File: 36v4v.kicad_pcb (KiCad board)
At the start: 2 copper layers, 85.1 x 48 mm, 47 parts, among them J1 Conn_01x03, J2 Conn_01x02, J3 Conn_01x02, J4 Conn_01x02, J5 Conn_01x02, J6 Conn_01x02, J7 Conn_01x02, U1 InnoSwitch3-CE, INN3162C, inS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

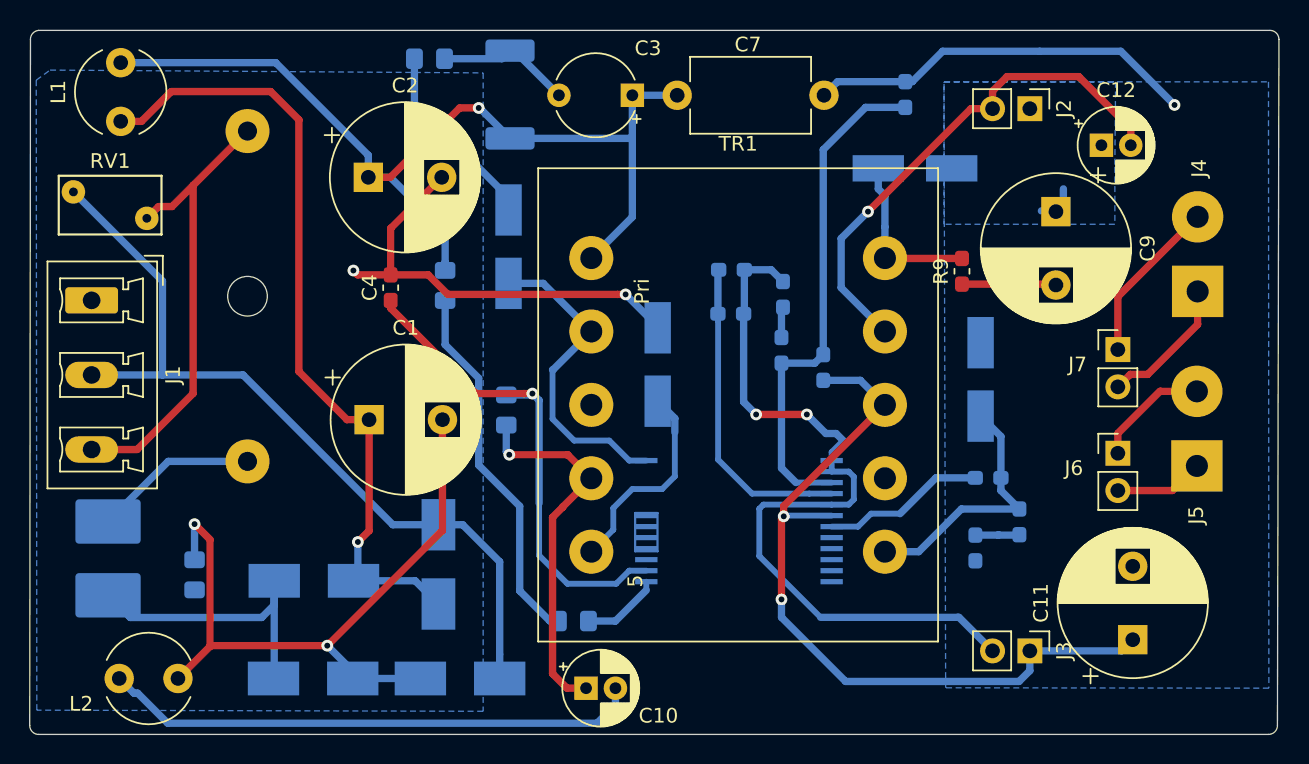
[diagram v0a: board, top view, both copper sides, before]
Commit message: Y-cap connected directly to DC pin of primary and secondary ground. BYPASS pin cap should be located as close as possible to BYPASS and SOURCE pins
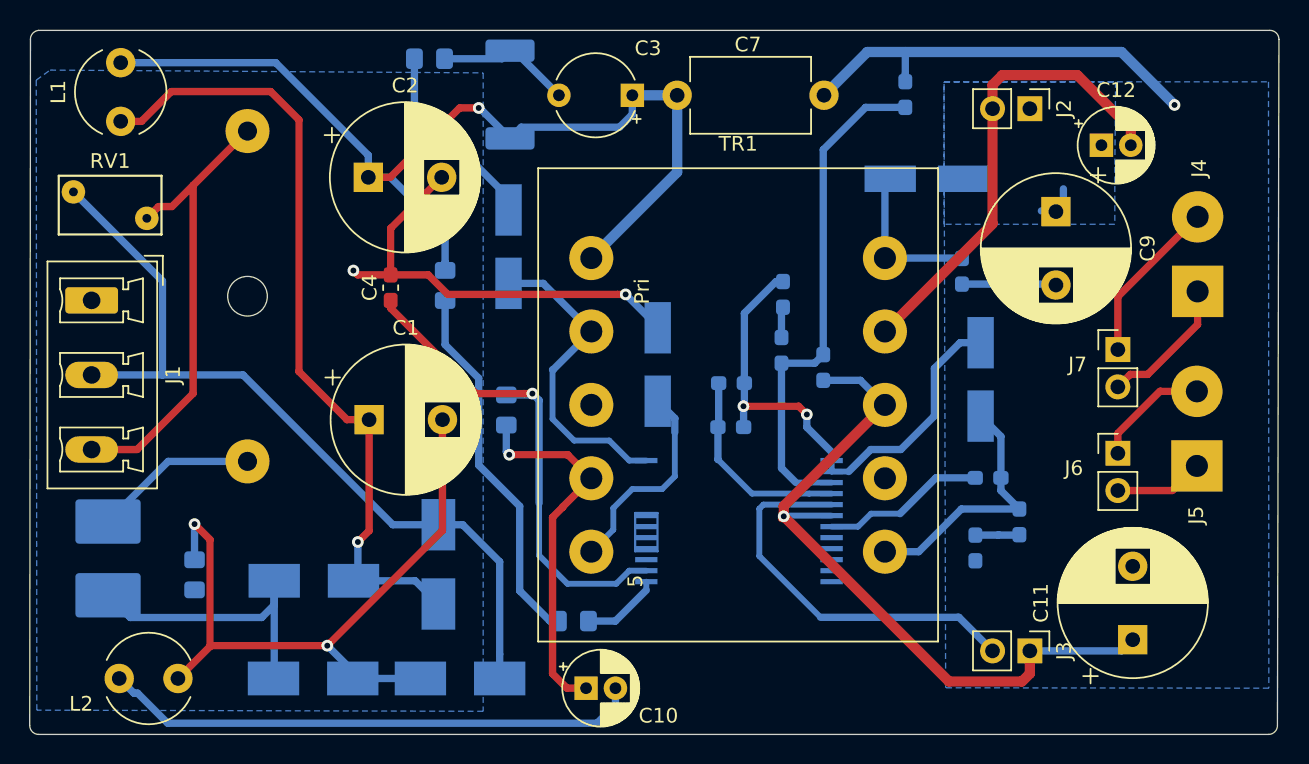
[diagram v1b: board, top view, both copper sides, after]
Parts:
- R9: moved to B.Cu
- moved C6 7.72 mm to (159.5, 95.2)
- moved C5 7.72 mm to (159.4, 98.2)
- moved D8 1.08 mm to (172.8, 81.3)
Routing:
- net GND: track 80.7 -> 91.7 mm
- net Net-(C5-Pad1): track 21.6 -> 13.9 mm
- net /4V: track 54.1 -> 49.4 mm, vias 2 -> 1
- net Net-(C2-Pad1): track 66.5 -> 69.7 mm
- net /GND1: track 35.2 -> 32.2 mm, vias 1 -> 0
- net Net-(D8-Pad2): track 12.6 -> 10.8 mm

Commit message: Maximize hatched area for heat sinking
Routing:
- added copper zone on B.Cu, net /sink
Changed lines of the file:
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@@
     (zones 0)
     (modules 47)
-    (nets 33)
+    (nets 34)
   )
   (page A4)
@@
     (user_trace_width 0.7)
     (trace_clearance 0.2)
-    (zone_clearance 0.7)
+    (zone_clearance 0.5)
     (zone_45_only no)
     (trace_min 0.2)
@@
   (net 31 "Net-(R11-Pad1)")
   (net 32 "Net-(C5-Pad1)")
+  (net 33 /sink)
   (net_class Default "This is the default net class."
     (clearance 0.2)
@@
     (add_net "Net-(R5-Pad1)")
     (add_net "Net-(R7-Pad1)")
-    (add_net "Net-(U1-Pad10)")
-    (add_net "Net-(U1-Pad11)")
-    (add_net "Net-(U1-Pad12)")
-    (add_net "Net-(U1-Pad15)")
-    (add_net "Net-(U1-Pad16)")
-    (add_net "Net-(U1-Pad17)")
-    (add_net "Net-(U1-Pad18)")
-    (add_net "Net-(U1-Pad19)")
-    (add_net "Net-(U1-Pad8)")
-    (add_net "Net-(U1-Pad9)")
   )
   (module footprints:INN3162C-H1XX (layer B.Cu)
@@
       )
     )
+  )
+  (zone (net 33) (net_name /sink) (layer B.Cu) (hatch edge 0.508)
+    (connect_pads (clearance 0.5))
+    (min_thickness 0.254)
+    (fill yes (arc_segments 32) (thermal_gap 0.508) (thermal_bridge_width 0.508))
+    (polygon
+      (pts
+        (xy 159.004 116.2304) (xy 156.6672 116.2304) (xy 156.6672 106.5276) (xy 152.8572 106.5276) (xy 152.8572 103.9876)
+        (xy 159.004 103.9876)
+      )
+    )

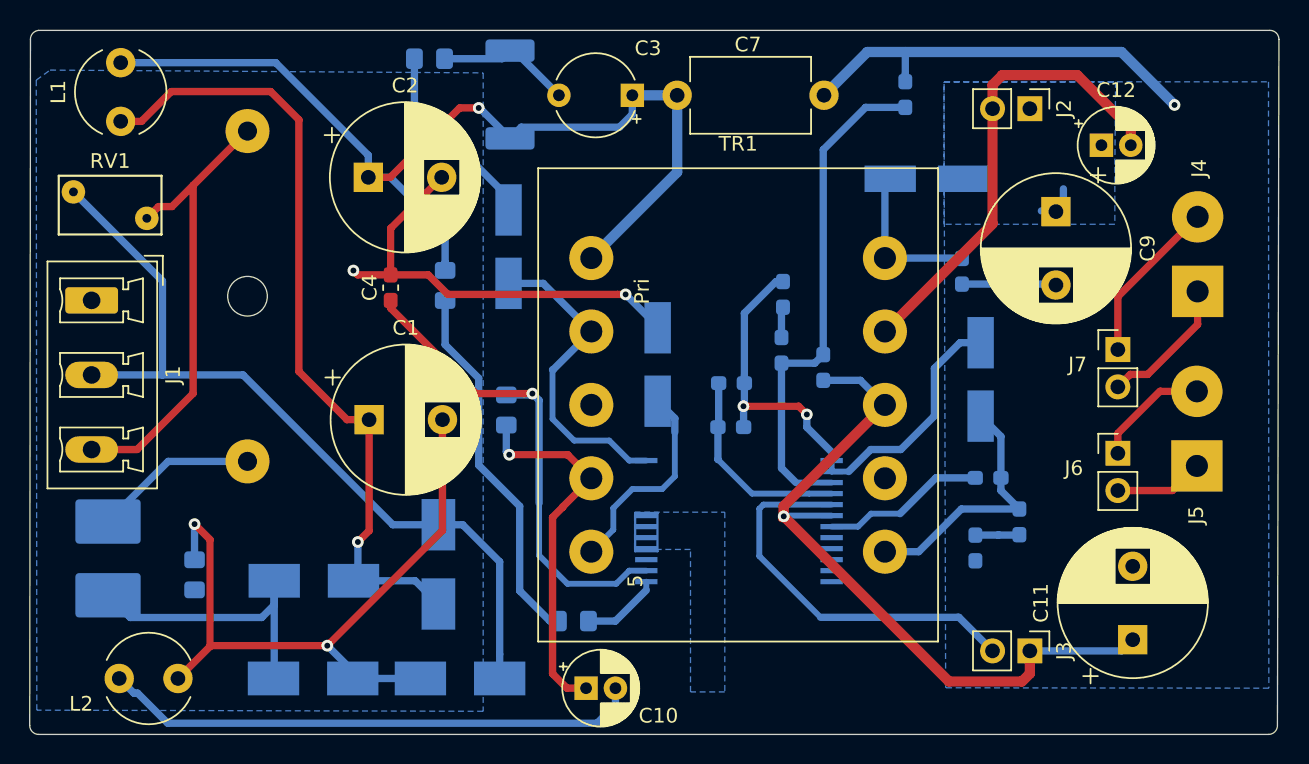
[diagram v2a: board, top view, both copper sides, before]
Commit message: Added ground/heatsink for Innoswitch. Added C14 as per Anil
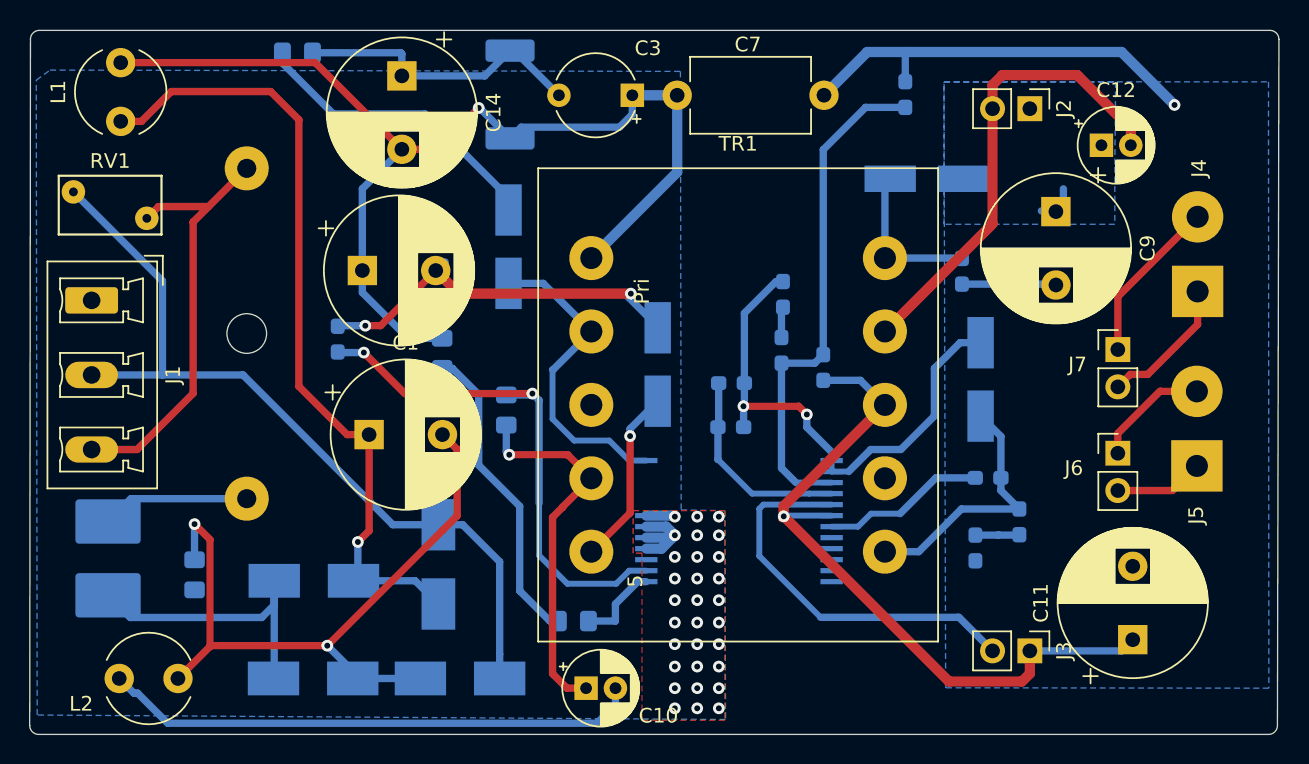
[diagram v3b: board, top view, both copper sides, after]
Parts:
- added C14: 10u 400V, Capacitor_THT:CP_Radial_D10.0mm_P5.00mm, F.Cu at (137.0, 74.3)
- C4: moved to B.Cu
- U1: footprint footprints:INN3162C-H1XX -> footprints:INN3162C-H1XX_
- moved R3 9.00 mm to (129.9, 72.7)
- moved C2 6.36 mm to (134.3, 87.5)
- moved C4 5.03 mm to (132.6, 92.2)
- moved R4 4.63 mm to (139.8, 93.2)
- moved F1 2.54 mm to (126.4, 80.6)
- moved C1 1.02 mm to (134.8, 98.7)
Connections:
- U1 pad 16: (no net) -> Earth
- U1 pad 17: (no net) -> Earth
- U1 pad 18: (no net) -> Earth
- U1 pad 19: (no net) -> Earth
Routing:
- net Net-(C14-Pad1): track 9.30 -> 21.1 mm
- net Net-(D5-Pad1): track 13.0 -> 20.7 mm
- net Net-(C14-Pad2): track 69.7 -> 75.5 mm
- net Net-(R4-Pad1): track 25.4 -> 21.2 mm
- net Earth: track 67.2 -> 71.1 mm, vias 2 -> 32
- net Net-(D6-Pad1): track 14.3 -> 12.1 mm, vias 0 -> 1
- net Net-(F1-Pad1): track 32.0 -> 29.9 mm
- net Net-(C4-Pad1): track 34.4 -> 36.2 mm, vias 1 -> 2
- net Net-(F1-Pad2): track 12.8 -> 11.7 mm
- added copper zone on F.Cu, net Earth
- removed copper zone on B.Cu, net /sink
